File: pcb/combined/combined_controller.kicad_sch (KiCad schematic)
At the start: 34 parts, among them J1 5V SCREEN, J10 PRESSURE, J11 XIAO D0-D6, J12 XIAO D7-5V, J7 24V IN, U10 LMR33630ADDAR, U6 ADS1115IDGST, U7 XIAO ESP32-S3 / SOCKETED

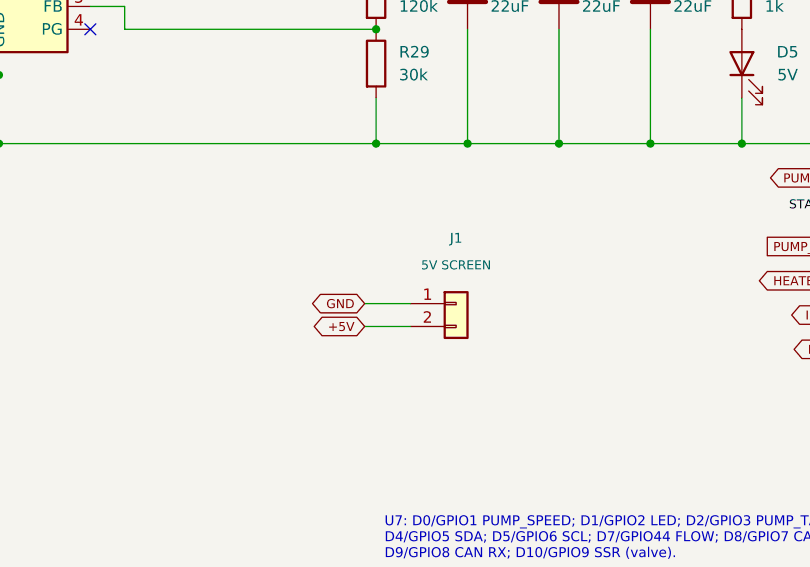
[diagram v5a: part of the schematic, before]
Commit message: Merge the combined screen 5 V and CAN connectors into one XH 4
J1 (5 V) and J5 (CAN) fed the same cable to the screen. One B4B-XH-A,
the part of J9, now carries 1 GND, 2 +5V, 3 CAN_L, 4 CAN_H and drops
C158012 from the extended parts. J1 takes the J9 placement corrections.

Co-Authored-By: Claude Opus 5.5 <noreply@anthropic.com>
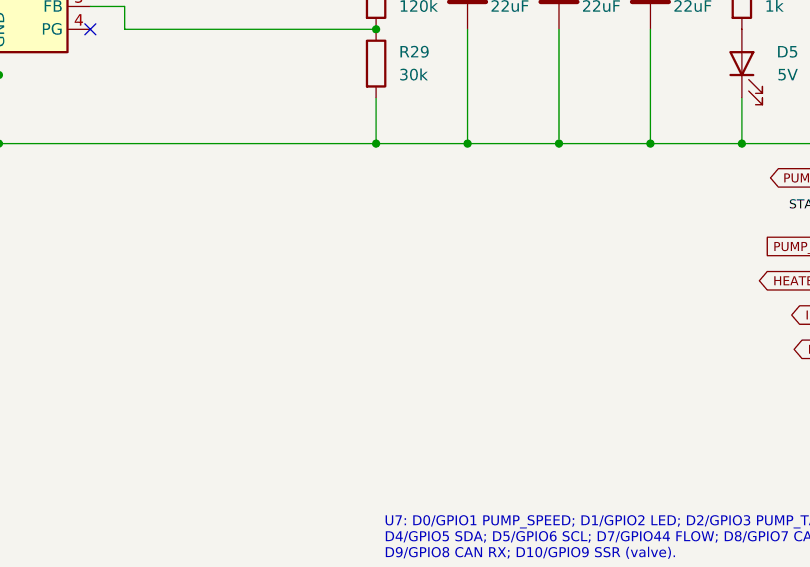
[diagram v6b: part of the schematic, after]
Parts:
- removed J1: 5V SCREEN, Connector_JST:JST_XH_B2B-XH-A_1x02_P2.50mm_Vertical, symbol Connector_Generic:Conn_01x02
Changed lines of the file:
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@@
-	(wire
-		(pts
-			(xy 182.88 81.28) (xy 177.8 81.28)
-		)
-		(stroke
-			(width 0)
-			(type default)
-		)
-	)
 	(wire
 		(pts
@@
 		(pts
 			(xy 383.54 102.87) (xy 383.54 107.95)
-		)
-		(stroke
-			(width 0)
-			(type default)
-		)
-	)
-	(wire
-		(pts
-			(xy 182.88 83.82) (xy 177.8 83.82)
 		)
 		(stroke
@@
 		(property "Intersheetrefs" "${INTERSHEET_REFS}"
 			(at 247.65 170.18 180)
-			(hide yes)
-			(show_name no)
-			(do_not_autoplace no)
-			(effects
-				(font
-					(size 1 1)
-				)
-			)
-		)
-	)
-	(global_label "+5V"
-		(shape bidirectional)
-		(at 177.8 83.82 180)
-		(effects
-			(font
-				(size 1 1)
-			)
-			(justify right)
-		)
-		(property "Intersheetrefs" "${INTERSHEET_REFS}"
-			(at 177.8 83.82 180)
 			(hide yes)
 			(show_name no)
@@
 	(global_label "GND"
 		(shape bidirectional)
-		(at 177.8 81.28 180)
-		(effects
-			(font
-				(size 1 1)
-			)
-			(justify right)
-		)
-		(property "Intersheetrefs" "${INTERSHEET_REFS}"
-			(at 177.8 81.28 180)
-			(hide yes)
-			(show_name no)
-			(do_not_autoplace no)
-			(effects
-				(font
-					(size 1 1)
-				)
-			)
-		)
-	)
-	(global_label "GND"
-		(shape bidirectional)
 		(at 287.02 71.12 0)
 		(effects
@@
 				)
 			)
-		)
-	)
-	(symbol
-		(lib_id "Connector_Generic:Conn_01x02")
-		(at 187.96 81.28 0)
-		(unit 1)
-		(body_style 1)
-		(exclude_from_sim no)
-		(in_bom yes)
-		(on_board yes)
-		(in_pos_files yes)
-		(dnp no)
-		(property "Reference" "J1"
-			(at 187.96 74.01 0)
-			(show_name no)
-			(do_not_autoplace no)
-			(effects
-				(font
-					(size 1.1 1.1)
-				)
-			)
-		)
-		(property "Value" "5V SCREEN"
-			(at 187.96 77.01 0)
-			(show_name no)
-			(do_not_autoplace no)
-			(effects
-				(font
-					(size 1 1)
-				)
-			)
-		)
-		(property "Footprint" "Connector_JST:JST_XH_B2B-XH-A_1x02_P2.50mm_Vertical"
-			(at 187.96 81.28 0)
-			(hide yes)
-			(show_name no)
-			(do_not_autoplace no)
-			(effects
-				(font
-					(size 1 1)
-				)
-			)
-		)
-		(property "Datasheet" ""
-			(at 187.96 81.28 0)
-			(hide yes)
-			(show_name no)
-			(do_not_autoplace no)
-			(effects
-				(font
-					(size 1 1)
-				)
-			)
-		)
-		(property "Description" "5 V out to the screen, along the CAN cable: 1 GND, 2 +5V"
-			(at 187.96 81.28 0)
-			(hide yes)
-			(show_name no)
-			(do_not_autoplace no)
-			(effects
-				(font
-					(size 1 1)
-				)
-			)
-		)
-		(property "MPN" "B2B-XH-A(LF)(SN)"
-			(at 187.96 81.28 0)
-			(hide yes)
-			(show_name no)
-			(do_not_autoplace no)
-			(effects
-				(font
-					(size 1 1)
-				)
-			)
-		)
-		(property "LCSC" "C158012"
-			(at 188.51 81.29 0)
-			(hide yes)
-			(show_name no)
-			(do_not_autoplace no)
-			(effects
-				(font
-					(size 1 1)
-				)
-			)
-		)
-		(pin "1"
-		)
-		(pin "2"
-		)
-		(instances
-			(project "combined"
-				(path "/a3ee807d-f8aa-4db3-ad94-73a886b6ed37/a559a4b4-f0a6-43cb-a3de-d40c2438cf59"
-					(reference "J1")
-					(unit 1)
-				)
-			)

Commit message: Lower the combined XIAO sockets to the 5 mm Hong Cheng header
J11/J12 move from the 8.5 mm hanxia socket (C22438157) to the Hong Cheng
HC-PM254-5.0H-1x7PZ (C27985232), the height Seeed uses on its XIAO boards.
The footprint takes the maker's 1.02 mm holes, its 18.18 x 2.4 mm body and
the LCSC 3D model. The supplier footprint matches the former one, so the
J11/J12 placement correction stays; the JLCPCB preview confirmed it.

Co-Authored-By: Claude Opus 5.5 <noreply@anthropic.com>
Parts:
- J11, J12: LCSC C22438157 -> C27985232; MPN HX PM2.54-1x7P ZC-Y -> HC-PM254-5.0H-1x7PZ
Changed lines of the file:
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@@
 			)
 		)
-		(property "MPN" "HX PM2.54-1x7P ZC-Y"
+		(property "MPN" "HC-PM254-5.0H-1x7PZ"
 			(at 257.81 165.1 0)
 			(hide yes)
@@
 			)
 		)
-		(property "LCSC" "C22438157"
+		(property "LCSC" "C27985232"
 			(at 257.81 165.1 0)
 			(hide yes)
@@
 			)
 		)
-		(property "MPN" "HX PM2.54-1x7P ZC-Y"
+		(property "MPN" "HC-PM254-5.0H-1x7PZ"
 			(at 293.37 165.1 0)
 			(hide yes)
@@
 			)
 		)
-		(property "LCSC" "C22438157"
+		(property "LCSC" "C27985232"
 			(at 293.37 165.1 0)
 			(hide yes)

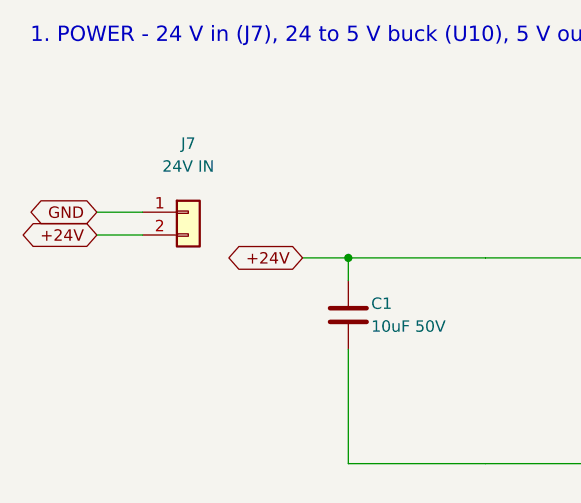
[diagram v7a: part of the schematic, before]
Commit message: Turn J7 so its plug latch faces south, like J8
The HT396K plug is 2.6 mm deeper than its header on the latch side. With
J7 turned 180 degrees, both 24 V and boiler plugs latch out through the
south wall of the enclosure. Its pins are swapped in the schematic so GND
stays on the left, next to U10. Adds the Kefa HT396K plug drawings.

Co-Authored-By: Claude Opus 5.5 <noreply@anthropic.com>
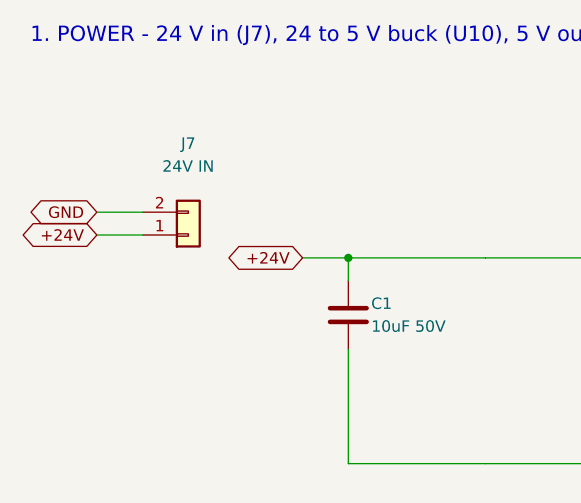
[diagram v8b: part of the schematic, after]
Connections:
- net +24V: now also J7.1 (Pin_1); no longer J7.2 (Pin_2)
- net GND: now also J7.2 (Pin_2); no longer J7.1 (Pin_1)
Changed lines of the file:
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@@
 	(symbol
 		(lib_id "Connector_Generic:Conn_01x02")
-		(at 35.56 35.56 0)
+		(at 35.56 38.1 0)
+		(mirror x)
 		(unit 1)
 		(body_style 1)
